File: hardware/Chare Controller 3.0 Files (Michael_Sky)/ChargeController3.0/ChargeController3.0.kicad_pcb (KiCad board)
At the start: 2 copper layers, 90 parts, among them J10 SOL_TEST_01x01_Pin, J11 GND_TEST_01x01_Pin, J13 Conn-1x2, J14 Conn-1x2, J15 Conn-1x2, J17 SCL_MAS_01x01_Pin, J18 SDA_MAS_01x01_Pin, J19 SYS-1x2, J2 SP_01x02_Pin, J3 BATT_TEST_01x01_Pin, J4 3.3V_PULLUP_01x02_Pin, J5 BATT_01x02_Pin, J6 Conn-1x2, J7 Conn-1x2, J8 Conn-1x2, J9 SYS_TEST_01x01_Pin, Q1 SI2318CDS-T1-GE3, Q10 SI2318CDS-T1-GE3, Q11 SI2318CDS-T1-GE3, Q13 SI2318CDS-T1-GE3, Q2 SI2318CDS-T1-GE3, Q3 SI2318CDS-T1-GE3, Q4 SI2318CDS-T1-GE3, Q5 AONS66614, Q6 AONS66614, Q7 AONS66614, Q8 AONS66614, Q9 SI2318CDS-T1-GE3, SW1 100SP1T1B1M1QEH, U1 BQ25756ERRVR

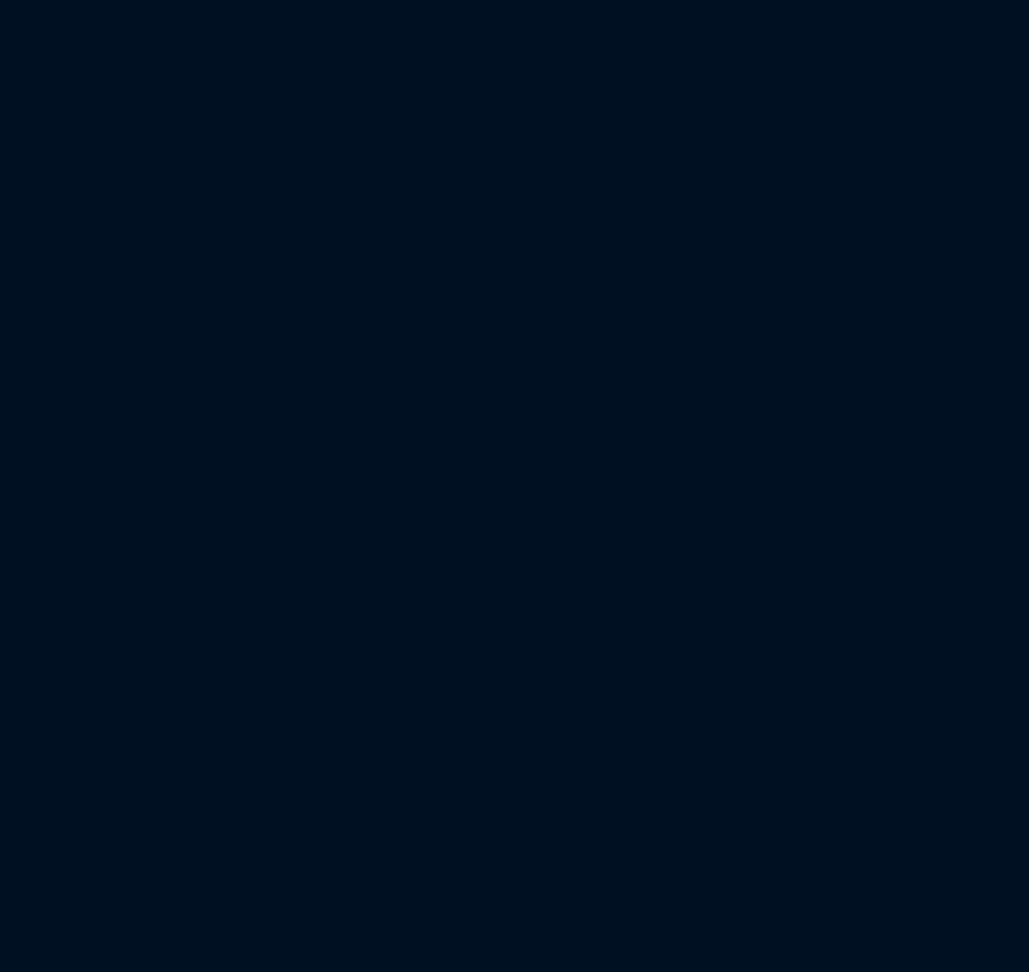
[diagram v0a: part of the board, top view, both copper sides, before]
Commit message: Added header pins and started labelling outputs
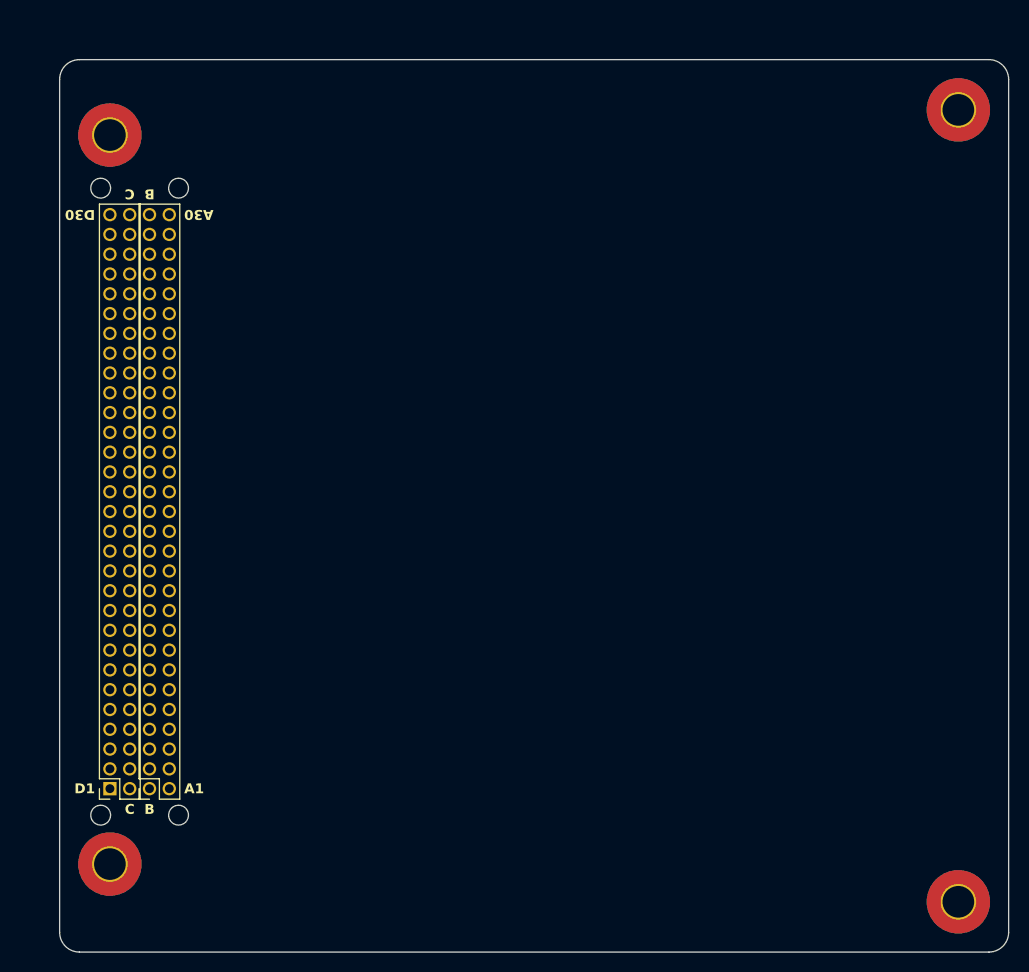
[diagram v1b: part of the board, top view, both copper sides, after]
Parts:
- added H1: MountingHole_Pad, MountingHole:MountingHole_3.2mm_M3_Pad_TopBottom, F.Cu at (102.8, 59.0)
- added H2: MountingHole_Pad, MountingHole:MountingHole_3.2mm_M3_Pad_TopBottom, F.Cu at (188.5, 56.5)
- added H3: MountingHole_Pad, MountingHole:MountingHole_3.2mm_M3_Pad_TopBottom, F.Cu at (102.8, 132.7)
- added H4: MountingHole_Pad, MountingHole:MountingHole_3.2mm_M3_Pad_TopBottom, F.Cu at (188.5, 136.5)
- added H5: MountingHole, MountingHole:MountingHole_2mm, F.Cu at (101.8, 64.4)
- added H6: MountingHole, MountingHole:MountingHole_2mm, F.Cu at (109.7, 64.4)
- added H7: MountingHole, MountingHole:MountingHole_2mm, F.Cu at (101.8, 127.8)
- added H8: MountingHole, MountingHole:MountingHole_2mm, F.Cu at (109.7, 127.8)
- added J1: Conn_02x30_Row_Letter_First, Connector_PinSocket_2.00mm:PinSocket_2x30_P2.00mm_Vertical, F.Cu at (106.8, 125.1)
- added J2: Conn_02x30_Row_Letter_First, Connector_PinSocket_2.00mm:PinSocket_2x30_P2.00mm_Vertical, F.Cu at (102.8, 125.1)
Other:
- board outline added: 95.9 x 90.2 mm
- board text added: "A1"
- board text added: "A30"
- board text added: "B"
- board text added: "C"
- board text added: "D1"
- board text added: "D30"

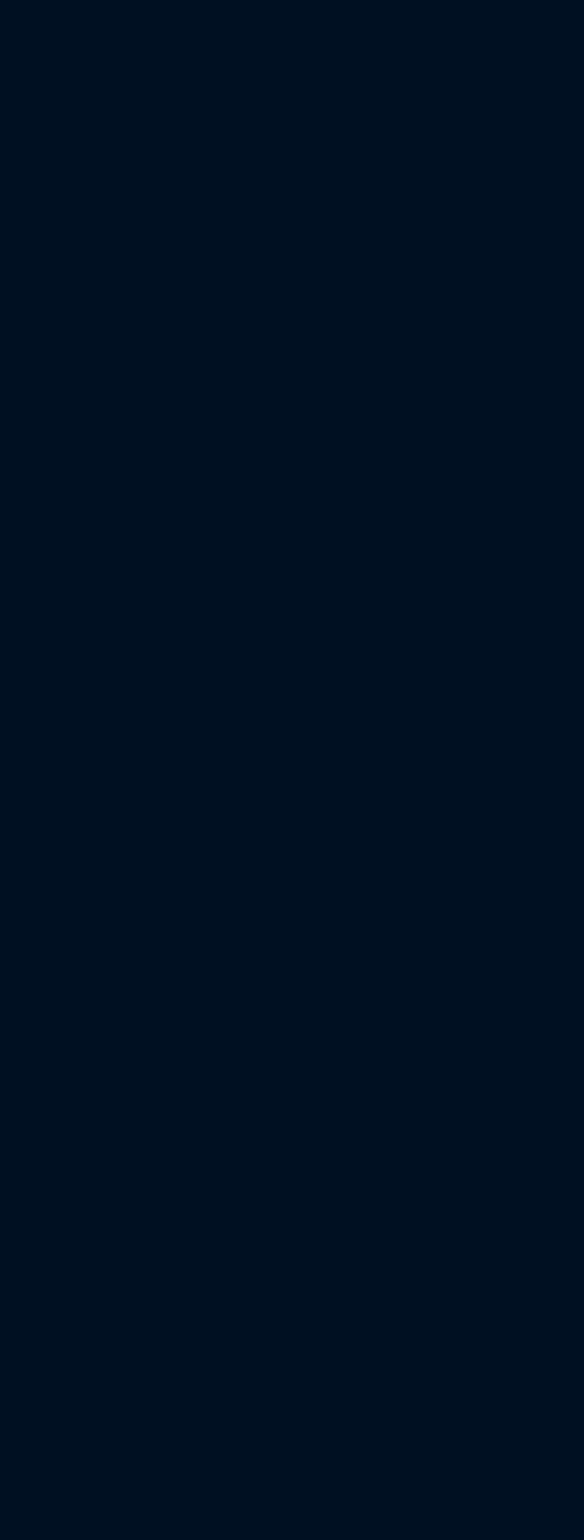
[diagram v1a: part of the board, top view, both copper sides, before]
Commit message: Formatting
Added schematic template from librecube, attempted to fix footprint template file path issues by copying over footprints into current project library
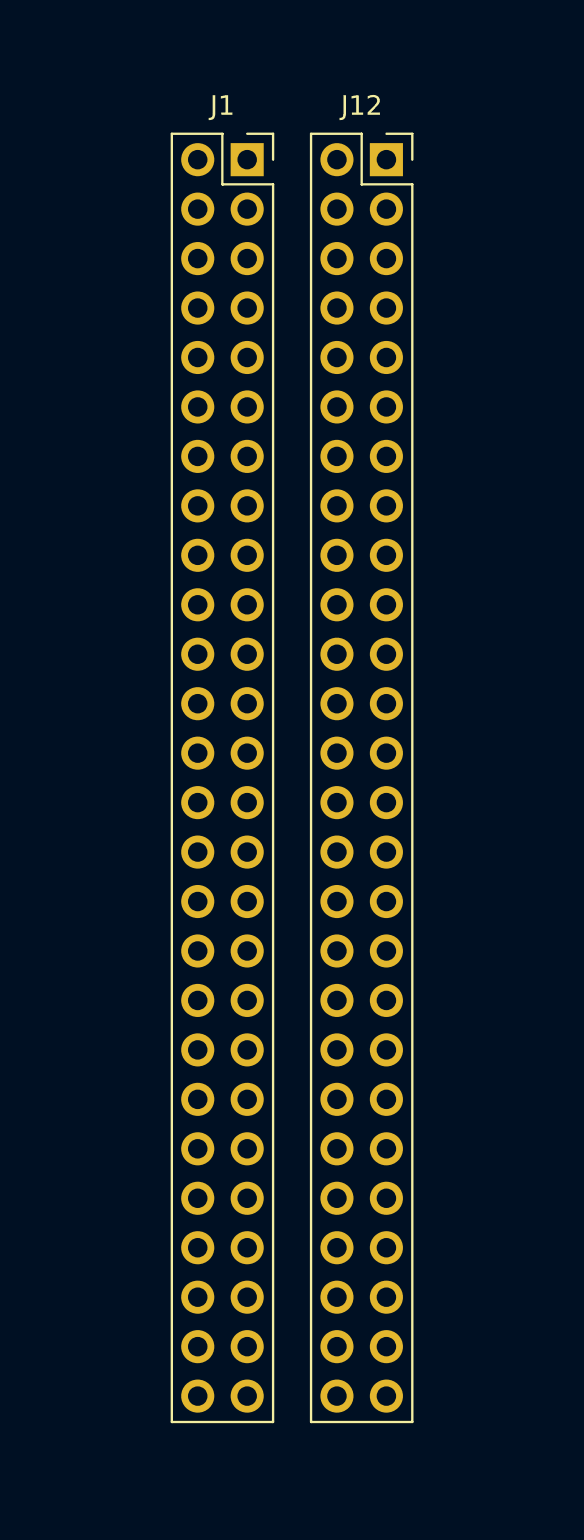
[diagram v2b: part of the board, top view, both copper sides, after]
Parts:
- added J1: Conn_02x26_Odd_Even, Connector_PinSocket_2.54mm:PinSocket_2x26_P2.54mm_Vertical, F.Cu at (74.8, 4.44)
- added J12: Conn_02x26_Odd_Even, Connector_PinSocket_2.54mm:PinSocket_2x26_P2.54mm_Vertical, F.Cu at (82.0, 4.44)

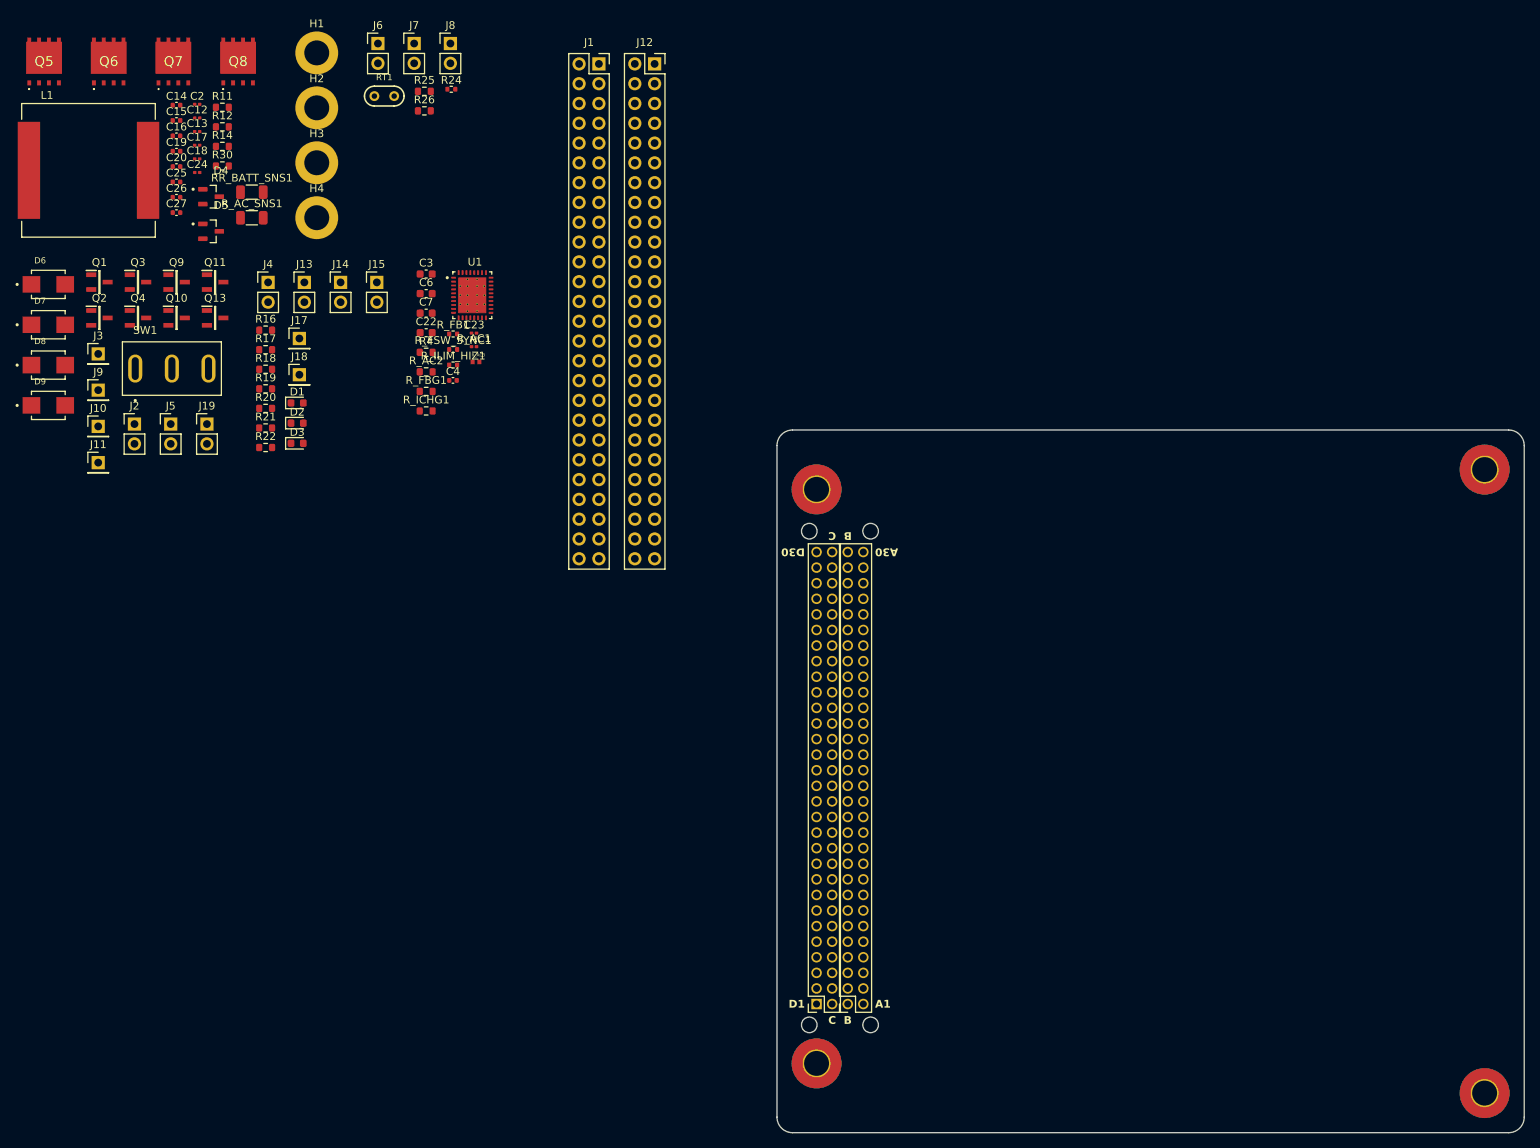
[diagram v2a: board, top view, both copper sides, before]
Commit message: added pins and pcb template
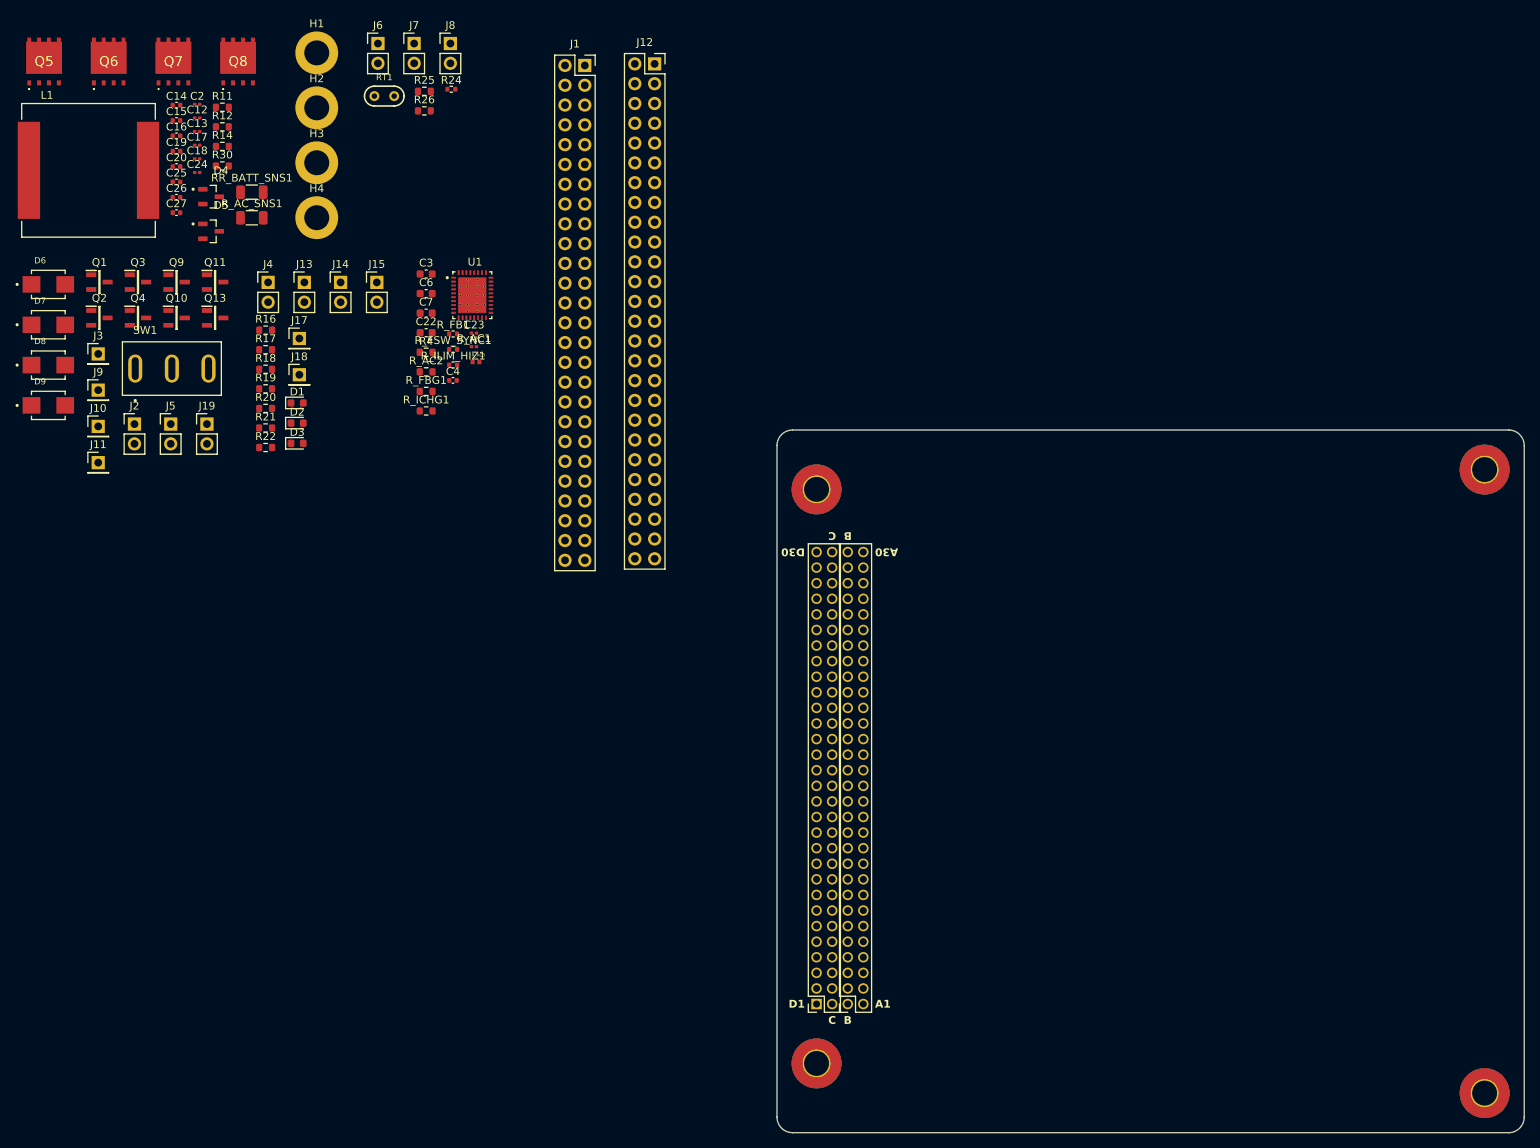
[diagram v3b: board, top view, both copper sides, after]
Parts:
- removed H5, H6, H7, H8: MountingHole, MountingHole:MountingHole_2mm
- moved J1 1.82 mm to (73.0, 4.64)
